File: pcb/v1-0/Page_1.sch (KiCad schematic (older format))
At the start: 64 parts, among them J1 Conn_01x04, J2 Conn_01x01, J3 Conn_02x02_Odd_Even, J4 Conn_01x04, J5 10118194-0001LF, J6 Conn_02x03_Odd_Even, U1 ATtiny3216-S, U2 SI7211-B-00-IV

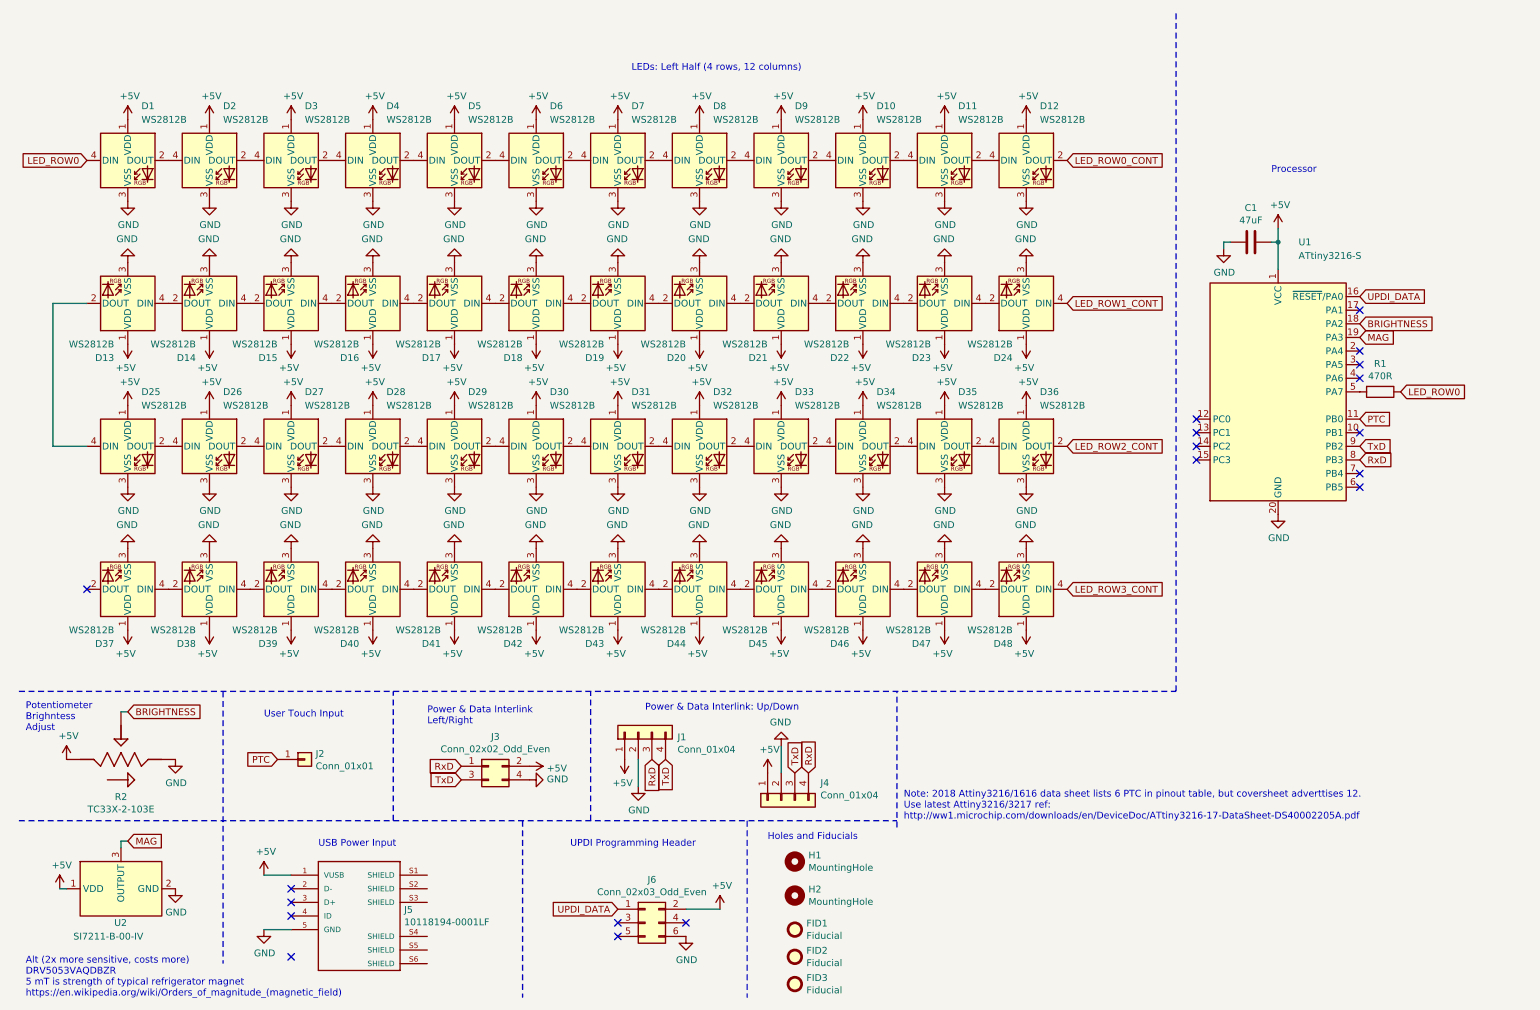
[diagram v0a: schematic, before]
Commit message: link schematic leds to layout
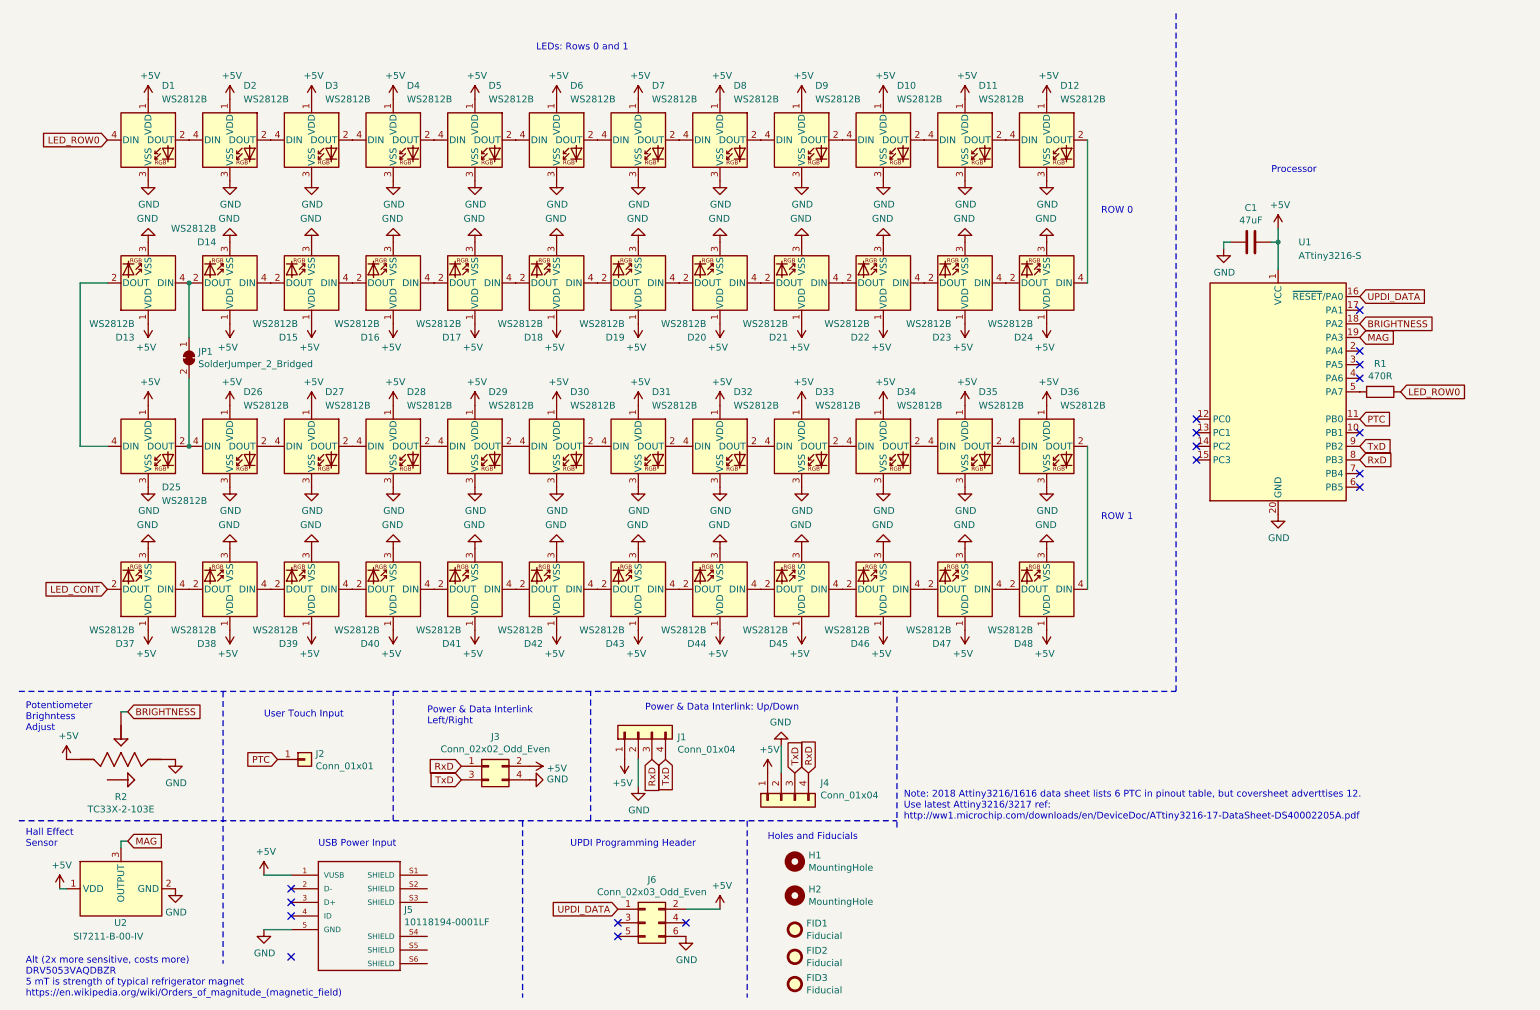
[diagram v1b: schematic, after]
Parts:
- added JP1: SolderJumper_2_Bridged, Jumper:SolderJumper-2_P1.3mm_Bridged_RoundedPad1.0x1.5mm, symbol Jumper:SolderJumper_2_Bridged
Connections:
- net LED_ROW1_CONT is gone; now on an unnamed net: D24.4 (DIN)
- net LED_ROW3_CONT is gone; now on an unnamed net: D48.4 (DIN)
- net at D13.4 (DIN), D14.2 (DOUT): now also JP1.1 (A)
- net at D25.2 (DOUT), D26.4 (DIN): now also JP1.2 (B)
- net LED_CONT: now reaches D37.2 (DOUT)
- net LED_ROW0_CONT: no longer names the net of D12.2 (DOUT)
- net LED_ROW2_CONT: no longer names the net of D36.2 (DOUT)
- no-connect marks 19 -> 18
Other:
- note added: "Hall Effect\nSensor"
- note added: "LEDs: Rows 0 and 1"
- note added: "ROW 0"
- note added: "ROW 1"
- note removed: "LEDs: Left Half (4 rows, 12 columns)"
- moved on the sheet: D1, D10, D11, D12, D13, D14, D15, D16, D17, D18, D19, D2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

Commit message: consider program over custom USB and remove 100 mil UPDI header
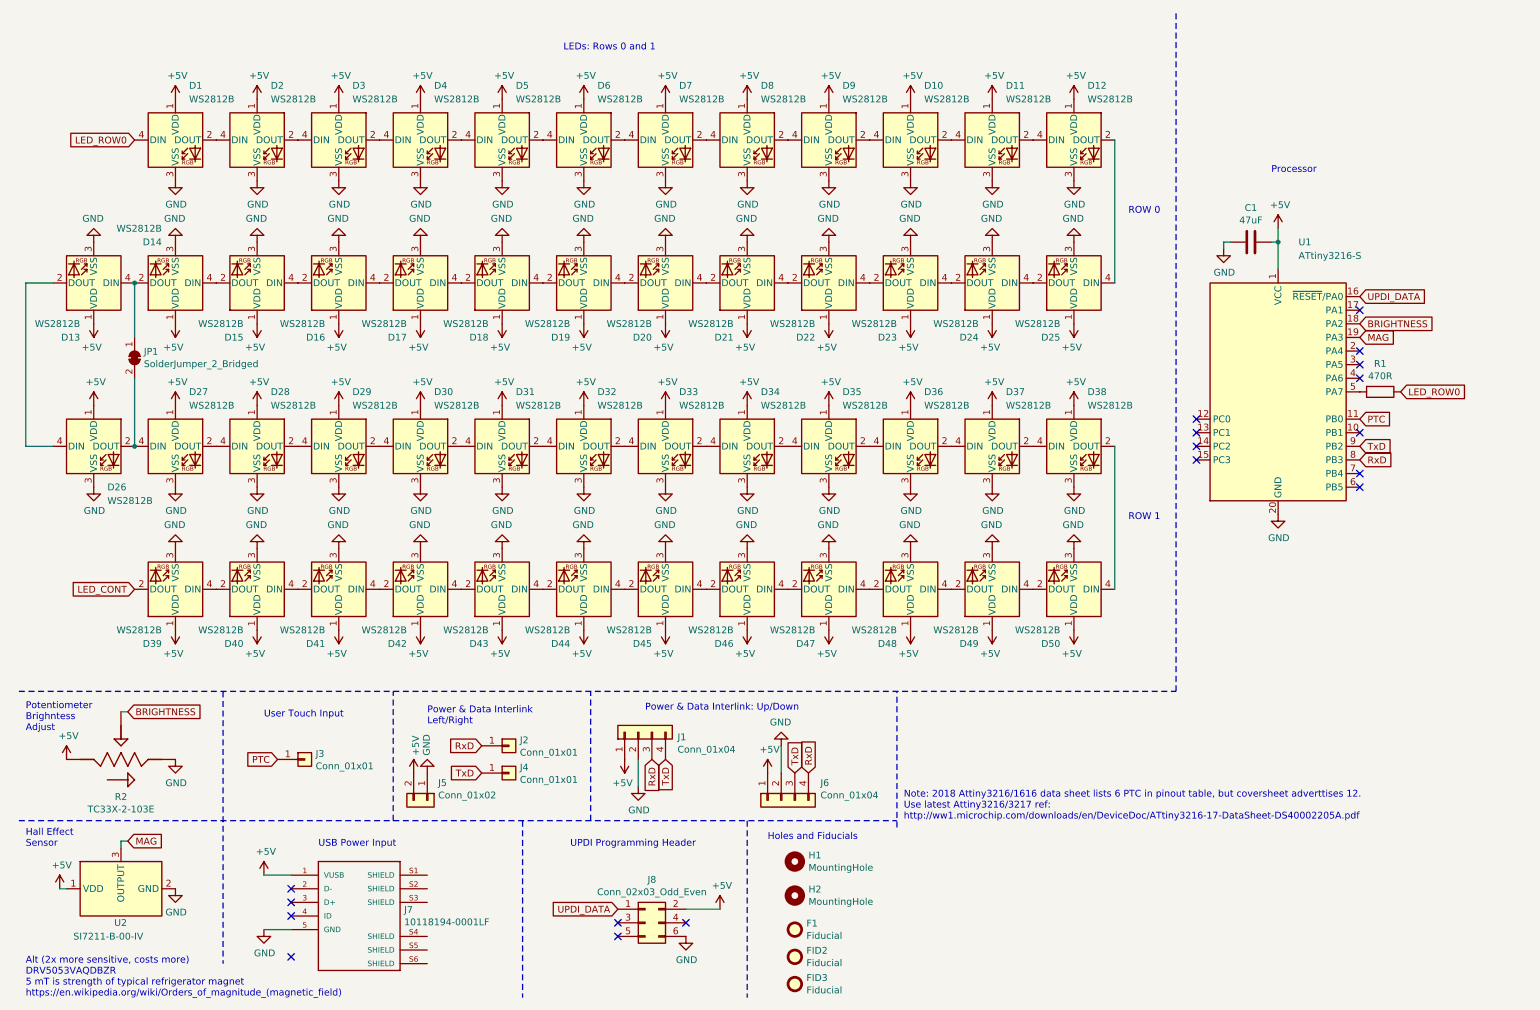
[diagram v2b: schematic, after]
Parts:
- removed J3: Conn_02x02_Odd_Even, Connector_PinHeader_2.54mm:PinHeader_2x02_P2.54mm_Vertical, symbol Connector_Generic:Conn_02x02_Odd_Even
- added D13, D28: WS2812B, WS2812B:LED_WS2812B_PLCC4_5.0x5.0mm_P3.2mm, symbol LED:WS2812B
- added J2, J4: Conn_01x01, Connector_PinHeader_2.54mm:PinHeader_1x01_P2.54mm_Vertical, symbol Connector_Generic:Conn_01x01
- added J5: Conn_01x02, Connector_PinHeader_2.54mm:PinHeader_1x02_P2.54mm_Vertical, symbol Connector_Generic:Conn_01x02
- renumbered D13 to D15, D15 to D16, D16 to D17, D17 to D18, D18 to D19, D19 to D20, D20 to D21, D21 to D22, D22 to D23, D23 to D24, D24 to D25, D25 to D26, D26 to D27, D27 to D29, D28 to D30, D29 to D31, D30 to D32, D31 to D33, D32 to D34, D33 to D35, D34 to D36, D35 to D37, D36 to D38, D37 to D39, D38 to D40, D39 to D41, D40 to D42, D41 to D43, D42 to D44, D43 to D45, D44 to D46, D45 to D47, D46 to D48, D47 to D49, D48 to D50, FID1 to F1, J2 to J3, J4 to J6, J5 to J7, J6 to J8
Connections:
- net +5V: now also D13.1 (VDD), D28.1 (VDD), J5.2 (Pin_2)
- net GND: now also D13.3 (VSS), D28.3 (VSS), J5.1 (Pin_1)
- net RxD: now also J2.1 (Pin_1)
- net TxD: now also J4.1 (Pin_1)
- net at D14.2 (DOUT), JP1.1 (A): now also D13.4 (DIN); no longer D15.4 (DIN)
- net at D14.4 (DIN): now also D15.2 (DOUT); no longer D16.2 (DOUT)
- net at D27.2 (DOUT): now also D28.4 (DIN); no longer D29.4 (DIN)
- net at D26.4 (DIN): now also D13.2 (DOUT); no longer D15.2 (DOUT)
- new net: D15.4 (DIN), D16.2 (DOUT)
- new net: D28.2 (DOUT), D29.4 (DIN)
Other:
- moved on the sheet: D1, D10, D11, D12, D14, D15, D16, D17, D18, D19, D2, D20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

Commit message: compontnets placedr
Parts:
- added S1: DS05-127-2-04BK-SMT-TR, SW_DS05-127-2-04BK-SMT-TR, symbol DS05-127-2-04BK-SMT-TR:DS05-127-2-04BK-SMT-TR
- renumbered FID2 to FID1, FID3 to FID2
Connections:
- net GND: now also S1.2B, S1.3B, S1.4B
- net UPDI_DATA: now also S1.1B
- net USB_UPDI: now reaches J7.4 (ID)
- net USB_UPDI: now also S1.1A
- net SW1: now reaches U1.2 (PA4)
- net SW1: now also S1.2A
- net SW2: now reaches U1.3 (PA5)
- net SW2: now also S1.3A
- net SW3: now reaches U1.4 (PA6)
- net SW3: now also S1.4A
- no-connect marks 18 -> 14
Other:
- note added: "DIP Switches"
- moved on the sheet: R1
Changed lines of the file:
@@
 $EndComp
 $Comp
-L power:GND #PWR0116
+L power:GND #PWR0117
 U 1 1 5F0CEA76
 P 2300 7250
-F 0 "#PWR0116" H 2300 7000 50  0001 C CNN
+F 0 "#PWR0117" H 2300 7000 50  0001 C CNN
 F 1 "GND" H 2305 7077 50  0000 C CNN
 F 2 "" H 2300 7250 50  0001 C CNN
@@
 $EndComp
 $Comp
-L power:+5V #PWR0112
+L power:+5V #PWR0113
 U 1 1 5F0CEA7C
 P 2300 6850
-F 0 "#PWR0112" H 2300 6700 50  0001 C CNN
+F 0 "#PWR0113" H 2300 6700 50  0001 C CNN
 F 1 "+5V" H 2315 7023 50  0000 C CNN
 F 2 "" H 2300 6850 50  0001 C CNN
@@
 UPDI_DATA
 $Comp
-L power:+5V #PWR0115
+L power:+5V #PWR0116
 U 1 1 5F0CEA97
 P 5650 7100
-F 0 "#PWR0115" H 5650 6950 50  0001 C CNN
+F 0 "#PWR0116" H 5650 6950 50  0001 C CNN
 F 1 "+5V" H 5665 7273 50  0000 C CNN
 F 2 "" H 5650 7100 50  0001 C CNN
@@
 	5650 7100 5400 7100
 $Comp
-L power:GND #PWR0117
+L power:GND #PWR0118
 U 1 1 5F0CEA9E
 P 5400 7300
-F 0 "#PWR0117" H 5400 7050 50  0001 C CNN
+F 0 "#PWR0118" H 5400 7050 50  0001 C CNN
 F 1 "GND" H 5405 7127 50  0000 C CNN
 F 2 "" H 5400 7300 50  0001 C CNN
@@
 $EndComp
 $Comp
-L Mechanical:Fiducial FID2
+L Mechanical:Fiducial FID1
 U 1 1 5F0CEAB1
 P 6200 7450
-F 0 "FID2" H 6285 7496 50  0000 L CNN
+F 0 "FID1" H 6285 7496 50  0000 L CNN
 F 1 "Fiducial" H 6285 7405 50  0000 L CNN
 F 2 "Fiducial:Fiducial_1mm_Mask2mm" H 6200 7450 50  0001 C CNN
@@
 $EndComp
 $Comp
-L Mechanical:Fiducial FID3
+L Mechanical:Fiducial FID2
 U 1 1 5F0CEAB7
 P 6200 7650
-F 0 "FID3" H 6285 7696 50  0000 L CNN
+F 0 "FID2" H 6285 7696 50  0000 L CNN
 F 1 "Fiducial" H 6285 7605 50  0000 L CNN
 F 2 "Fiducial:Fiducial_1mm_Mask2mm" H 6200 7650 50  0001 C CNN
@@
 Alt (2x more sensitive, costs more)\nDRV5053VAQDBZR\n5 mT is strength of typical refrigerator magnet\nhttps://en.wikipedia.org/wiki/Orders_of_magnitude_(magnetic_field)
 $Comp
-L power:GND #PWR0114
+L power:GND #PWR0115
 U 1 1 5F0CEADF
 P 1650 6950
-F 0 "#PWR0114" H 1650 6700 50  0001 C CNN
+F 0 "#PWR0115" H 1650 6700 50  0001 C CNN
 F 1 "GND" H 1655 6777 50  0000 C CNN
 F 2 "" H 1650 6950 50  0001 C CNN
@@
 $EndComp
 $Comp
-L power:+5V #PWR0113
+L power:+5V #PWR0114
 U 1 1 5F0CEAE5
 P 800 6950
-F 0 "#PWR0113" H 800 6800 50  0001 C CNN
+F 0 "#PWR0114" H 800 6800 50  0001 C CNN
 F 1 "+5V" H 815 7123 50  0000 C CNN
 F 2 "" H 800 6950 50  0001 C CNN
@@
 MAG
 $Comp
-L power:GND #PWR0109
+L power:GND #PWR0110
 U 1 1 5F0CEAEC
 P 3500 6100
-F 0 "#PWR0109" H 3500 5850 50  0001 C CNN
+F 0 "#PWR0110" H 3500 5850 50  0001 C CNN
 F 1 "GND" V 3505 5972 50  0000 R CNN
 F 2 "" H 3500 6100 50  0001 C CNN
@@
 $EndComp
 $Comp
-L power:+5V #PWR0108
+L power:+5V #PWR0109
 U 1 1 5F0CEAF2
 P 3400 6100
-F 0 "#PWR0108" H 3400 5950 50  0001 C CNN
+F 0 "#PWR0109" H 3400 5950 50  0001 C CNN
 F 1 "+5V" V 3415 6228 50  0000 L CNN
 F 2 "" H 3400 6100 50  0001 C CNN
@@
 RxD
 $Comp
-L power:+5V #PWR0107
+L power:+5V #PWR0108
 U 1 1 5F0CEB0C
 P 4950 6000
-F 0 "#PWR0107" H 4950 5850 50  0001 C CNN
+F 0 "#PWR0108" H 4950 5850 50  0001 C CNN
 F 1 "+5V" H 4965 6173 50  0000 C CNN
 F 2 "" H 4950 6000 50  0001 C CNN
@@
 $EndComp
 $Comp
-L power:+5V #PWR0110
+L power:+5V #PWR0111
 U 1 1 5F0CEB12
 P 6000 6100
-F 0 "#PWR0110" H 6000 5950 50  0001 C CNN
+F 0 "#PWR0111" H 6000 5950 50  0001 C CNN
 F 1 "+5V" H 6015 6273 50  0000 C CNN
 F 2 "" H 6000 6100 50  0001 C CNN
@@
 $EndComp
 $Comp
-L power:GND #PWR0111
+L power:GND #PWR0112
 U 1 1 5F0CEB18
 P 5050 6200
-F 0 "#PWR0111" H 5050 5950 50  0001 C CNN
+F 0 "#PWR0112" H 5050 5950 50  0001 C CNN
 F 1 "GND" H 5055 6027 50  0000 C CNN
 F 2 "" H 5050 6200 50  0001 C CNN
@@
 $EndComp
 $Comp
-L power:GND #PWR0104
+L power:GND #PWR0105
 U 1 1 5F0CEB1E
 P 6100 5900
-F 0 "#PWR0104" H 6100 5650 50  0001 C CNN
+F 0 "#PWR0105" H 6100 5650 50  0001 C CNN
 F 1 "GND" H 6105 5727 50  0000 C CNN
 F 2 "" H 6100 5900 50  0001 C CNN
@@
 NoConn ~ 2500 6950
 NoConn ~ 2500 7050
-NoConn ~ 2500 7150
 NoConn ~ 2500 7450
 $Comp
-L power:GND #PWR0106
+L power:GND #PWR0107
 U 1 1 5F0CEB6F
 P 1650 6000
-F 0 "#PWR0106" H 1650 5750 50  0001 C CNN
+F 0 "#PWR0107" H 1650 5750 50  0001 C CNN
 F 1 "GND" H 1655 5827 50  0000 C CNN
 F 2 "" H 1650 6000 50  0001 C CNN
@@
 $EndComp
 $Comp
-L power:+5V #PWR0105
+L power:+5V #PWR0106
 U 1 1 5F0CEB75
 P 850 6000
-F 0 "#PWR0105" H 850 5850 50  0001 C CNN
+F 0 "#PWR0106" H 850 5850 50  0001 C CNN
 F 1 "+5V" H 865 6173 50  0000 C CNN
 F 2 "" H 850 6000 50  0001 C CNN
@@
 	-1   0    0    1
 $EndComp
-Text GLabel 10650 3300 2    50   Input ~ 0
+Text GLabel 10750 3700 2    50   Input ~ 0
 LED_ROW0
 $Comp
@@
 NoConn ~ 10350 4000
 NoConn ~ 10350 3600
-NoConn ~ 10350 3200
-NoConn ~ 10350 3100
-NoConn ~ 10350 3000
 NoConn ~ 10350 2700
 NoConn ~ 9150 3500
@@
 L Device:R R1
 U 1 1 5F0CEC00
-P 10500 3300
-F 0 "R1" V 10293 3300 50  0000 C CNN
-F 1 "470R" V 10384 3300 50  0000 C CNN
-F 2 "Resistor_SMD:R_0805_2012Metric" V 10430 3300 50  0001 C CNN
-F 3 "~" H 10500 3300 50  0001 C CNN
-	1    10500 3300
-	0    1    1    0
+P 10700 3500
+F 0 "R1" V 10493 3500 50  0000 C CNN
+F 1 "470R" V 10584 3500 50  0000 C CNN
+F 2 "Resistor_SMD:R_0805_2012Metric" V 10630 3500 50  0001 C CNN
+F 3 "~" H 10700 3500 50  0001 C CNN
+	1    10700 3500
+	-1   0    0    1
 $EndComp
 $Comp
@@
 	0    1    1    0
 $EndComp
+$Comp
+L DS05-127-2-04BK-SMT-TR:DS05-127-2-04BK-SMT-TR S1
+U 1 1 5F52CB4C
+P 10100 5500
+F 0 "S1" H 10100 6049 50  0000 C CNN
+F 1 "DS05-127-2-04BK-SMT-TR" H 10100 5958 50  0000 C CNN
+F 2 "SW_DS05-127-2-04BK-SMT-TR" H 10100 5500 50  0001 L BNN
+F 3 "V0.0" H 10100 5500 50  0001 L BNN
+F 4 "Manufacturer Recommendations" H 10100 5500 50  0001 L BNN "Field4"
+F 5 "2.60 mm" H 10100 5500 50  0001 L BNN "Field5"
+F 6 "CUI Inc." H 10100 5500 50  0001 L BNN "Field6"
+	1    10100 5500
+	1    0    0    -1
+$EndComp
+Text GLabel 2500 7150 0    50   Input ~ 0
+USB_UPDI
+Text GLabel 9800 5200 0    50   Input ~ 0
+USB_UPDI
+Text GLabel 10400 5200 2    50   Input ~ 0
+UPDI_DATA
+$Comp
+L power:GND #PWR0104
+U 1 1 5F541CCE
+P 10500 5850
+F 0 "#PWR0104" H 10500 5600 50  0001 C CNN
+F 1 "GND" H 10505 5677 50  0000 C CNN
+F 2 "" H 10500 5850 50  0001 C CNN
+F 3 "" H 10500 5850 50  0001 C CNN
+	1    10500 5850
+	1    0    0    -1
+$EndComp
+Wire Wire Line
+	10500 5850 10500 5800
+Wire Wire Line
+	10500 5400 10400 5400
+Wire Wire Line
+	10400 5600 10500 5600
+Connection ~ 10500 5600
+Wire Wire Line
+	10500 5600 10500 5400
+Wire Wire Line
+	10400 5800 10500 5800
+Connection ~ 10500 5800
+Wire Wire Line
+	10500 5800 10500 5600
+Text GLabel 9800 5400 0    50   Input ~ 0
+SW1
+Text GLabel 9800 5600 0    50   Input ~ 0
+SW2
+Text GLabel 9800 5800 0    50   Input ~ 0
+SW3
+Wire Wire Line
+	10700 3350 10700 3300
+Wire Wire Line
+	10700 3300 10350 3300
+Wire Wire Line
+	10750 3700 10700 3700
+Wire Wire Line
+	10700 3700 10700 3650
+Text GLabel 10350 3000 2    50   Input ~ 0
+SW1
+Text GLabel 10350 3100 2    50   Input ~ 0
+SW2
+Text GLabel 10350 3200 2    50   Input ~ 0
+SW3
+Text Notes 9850 4800 0    50   ~ 0
+DIP Switches
+Wire Notes Line
+	11200 4550 9000 4550
 $EndSCHEMATC

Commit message: pre-zone fill
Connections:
- net SW1: now also U1.4 (PA6); no longer U1.2 (PA4)
- net SW3: now also U1.2 (PA4); no longer U1.4 (PA6)
- no-connect marks 14 -> 19
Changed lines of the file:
@@
 NoConn ~ 2500 6950
 NoConn ~ 2500 7050
-NoConn ~ 2500 7450
 $Comp
 L power:GND #PWR0107
@@
 	10700 3700 10700 3650
 Text GLabel 10350 3000 2    50   Input ~ 0
-SW1
+SW3
 Text GLabel 10350 3100 2    50   Input ~ 0
 SW2
 Text GLabel 10350 3200 2    50   Input ~ 0
-SW3
+SW1
 Text Notes 9850 4800 0    50   ~ 0
 DIP Switches
 Wire Notes Line
 	11200 4550 9000 4550
+NoConn ~ 3500 6850
+NoConn ~ 3500 6950
+NoConn ~ 3500 7050
+NoConn ~ 3500 7300
+NoConn ~ 3500 7400
+NoConn ~ 3500 7500
 $EndSCHEMATC
